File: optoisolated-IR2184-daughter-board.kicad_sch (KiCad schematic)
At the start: 3 parts, among them J1 Conn_01x08_Pin, U1 IR2184, U2 6N137

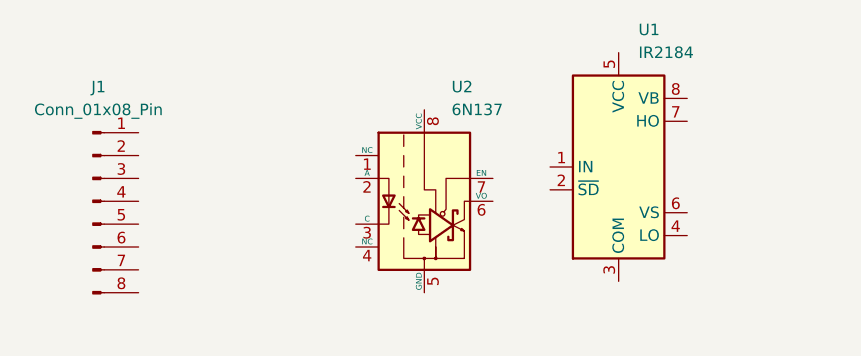
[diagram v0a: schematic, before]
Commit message: update dip packages
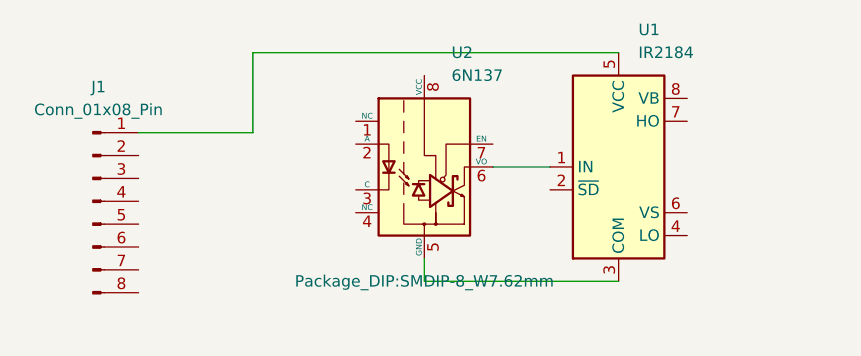
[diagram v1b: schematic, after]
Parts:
- J1: footprint (none) -> Connector_JST:JST_EH_B8B-EH-A_1x08_P2.50mm_Vertical
- U1: footprint (none) -> Package_SO:SOIC-8_3.9x4.9mm_P1.27mm
- U2: footprint Package_DIP:DIP-8_W7.62mm -> Package_DIP:SMDIP-8_W7.62mm
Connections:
- net at U1.1 (IN): now also U2.6 (VO)
- net at U1.3 (COM): now also U2.5 (GND)
- net at U1.5 (VCC): now also J1.1 (Pin_1)
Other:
- moved on the sheet: U2
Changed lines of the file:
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@@
 	(generator_version "8.0")
 	(paper "A4")
+	(wire
+		(pts
+			(xy 115.57 67.31) (xy 128.27 67.31)
+		)
+		(stroke
+			(width 0)
+			(type default)
+		)
+	)
+	(wire
+		(pts
+			(xy 128.27 67.31) (xy 128.27 58.42)
+		)
+		(stroke
+			(width 0)
+			(type default)
+		)
+	)
+	(wire
+		(pts
+			(xy 168.91 83.82) (xy 147.32 83.82)
+		)
+		(stroke
+			(width 0)
+			(type default)
+		)
+	)
+	(wire
+		(pts
+			(xy 154.94 71.12) (xy 161.29 71.12)
+		)
+		(stroke
+			(width 0)
+			(type default)
+		)
+	)
+	(wire
+		(pts
+			(xy 128.27 58.42) (xy 168.91 58.42)
+		)
+		(stroke
+			(width 0)
+			(type default)
+		)
+	)
+	(wire
+		(pts
+			(xy 147.32 83.82) (xy 147.32 81.28)
+		)
+		(stroke
+			(width 0)
+			(type default)
+		)
+	)
 	(symbol
 		(lib_id "Driver_FET:IR2184")
@@
 			)
 		)
-		(property "Footprint" ""
+		(property "Footprint" "Package_SO:SOIC-8_3.9x4.9mm_P1.27mm"
 			(at 168.91 71.12 0)
 			(effects
@@
 	(symbol
 		(lib_id "Isolator:6N137")
-		(at 147.32 74.93 0)
+		(at 147.32 71.12 0)
 		(unit 1)
 		(exclude_from_sim no)
@@
 		(fields_autoplaced yes)
 		(property "Reference" "U2"
-			(at 150.3365 62.23 0)
+			(at 150.3365 58.42 0)
 			(effects
 				(font
@@
 		)
 		(property "Value" "6N137"
-			(at 150.3365 64.77 0)
-			(effects
-				(font
-					(size 1.27 1.27)
-				)
-				(justify left)
-			)
-		)
-		(property "Footprint" "Package_DIP:DIP-8_W7.62mm"
-			(at 147.32 87.63 0)
-			(effects
-				(font
-					(size 1.27 1.27)
-				)
-				(hide yes)
+			(at 150.3365 60.96 0)
+			(effects
+				(font
+					(size 1.27 1.27)
+				)
+				(justify left)
+			)
+		)
+		(property "Footprint" "Package_DIP:SMDIP-8_W7.62mm"
+			(at 147.32 83.82 0)
+			(effects
+				(font
+					(size 1.27 1.27)
+				)
 			)
 		)
 		(property "Datasheet" "https://docs.broadcom.com/docs/AV02-0940EN"
-			(at 125.73 60.96 0)
+			(at 125.73 57.15 0)
 			(effects
 				(font
@@
 		)
 		(property "Description" "Single High Speed LSTTL/TTL Compatible Optocoupler with enable, dV/dt 1000/us, VCM 10, max 7V VCC, DIP-8"
-			(at 147.32 74.93 0)
+			(at 147.32 71.12 0)
 			(effects
 				(font
@@
 			)
 		)
-		(property "Footprint" ""
+		(property "Footprint" "Connector_JST:JST_EH_B8B-EH-A_1x08_P2.50mm_Vertical"
 			(at 110.49 74.93 0)
 			(effects

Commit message: placed most parts
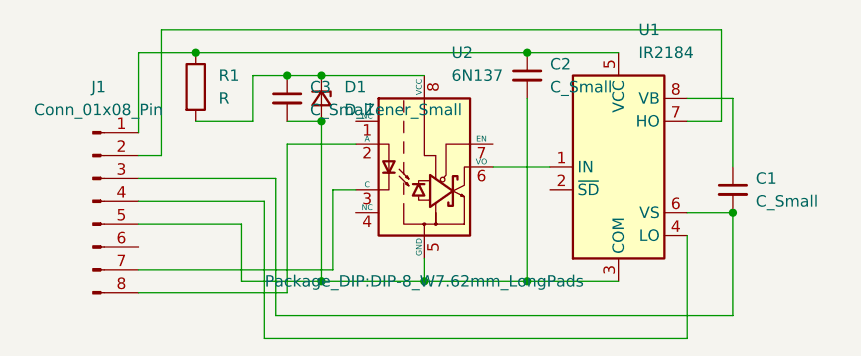
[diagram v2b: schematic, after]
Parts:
- added C1, C2, C3: C_Small, symbol Device:C_Small
- added D1: D_Zener_Small, symbol Device:D_Zener_Small
- added R1: R, symbol Device:R
- U1: footprint Package_SO:SOIC-8_3.9x4.9mm_P1.27mm -> Package_DIP:DIP-8_W7.62mm_LongPads
- U2: footprint Package_DIP:SMDIP-8_W7.62mm -> Package_DIP:DIP-8_W7.62mm_LongPads
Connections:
- net at U1.3 (COM), U2.5 (GND): now also J1.5 (Pin_5), C2.2, C3.2, D1.2 (A)
- net at U1.4 (LO): now also J1.4 (Pin_4)
- net at J1.1 (Pin_1), U1.5 (VCC): now also C2.1, R1.1
- net at U1.6 (VS): now also J1.3 (Pin_3), C1.2
- net at U1.7 (HO): now also J1.2 (Pin_2)
- net at U1.8 (VB): now also C1.1
- net at U2.2 (A): now also J1.8 (Pin_8)
- net at U2.3 (C): now also J1.7 (Pin_7)
- net at U2.8 (VCC): now also C3.1, D1.1 (K), R1.2
